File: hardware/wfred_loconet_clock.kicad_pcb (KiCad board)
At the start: 2 copper layers, 124 x 35 mm, 65 parts, among them IC201 ATMEGA328P-A, J301 Molex 95501-6669, K301 TERMINATION, K401 UART_ESP, K402 UART_AVR, P201 ISP, P401 ESP_BOOTLOAD, P501 CLOCK, Q301 BC817-40, Q302 BC817-40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

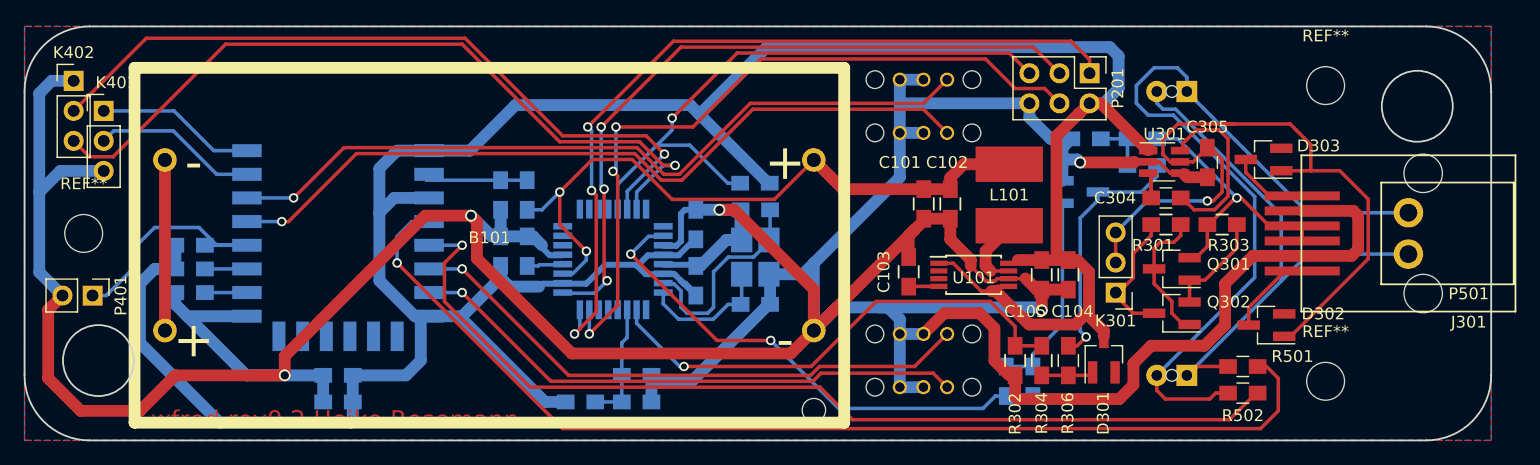
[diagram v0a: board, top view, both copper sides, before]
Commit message: Bugfix: Moved PCB mounting holes to correct corners
	(had been fitting for original FRED with UI on screw side,
	 which does not fit housing with battery cover)
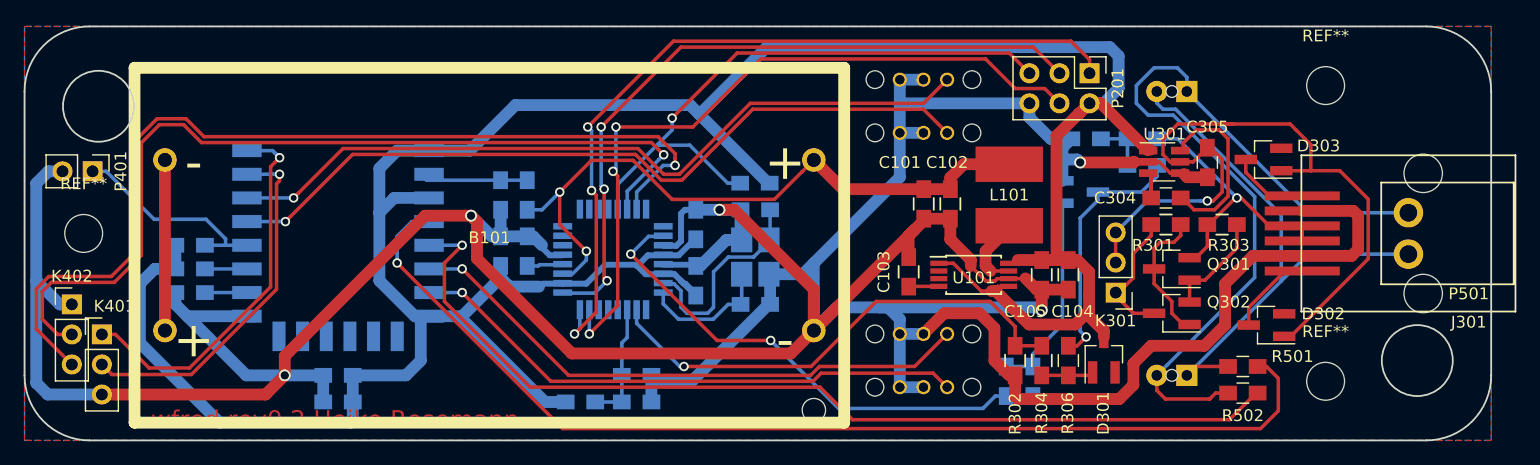
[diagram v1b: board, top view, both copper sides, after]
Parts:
- moved K401 18.9 mm to (76.5, 108.5)
- moved K402 18.9 mm to (74.0, 106.0)
- moved P401 10.5 mm to (75.8, 94.8)
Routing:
- net Net-(K401-Pad1): track 14.2 -> 32.5 mm, vias 0 -> 1
- net THIS_TXD: track 65.3 -> 81.0 mm
- net Net-(K401-Pad2): track 14.7 -> 30.0 mm, vias 0 -> 1
- net THIS_RXD: track 62.6 -> 76.3 mm
- net GND: track 393.8 -> 381.9 mm
- net Net-(P401-Pad1): track 22.0 -> 18.4 mm
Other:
- outline, holes or cut-outs redrawn

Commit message: Bugfix: Increased SW313 mounting hole clearance
	plus made GND fill distance to PCB edges larger for panelizing
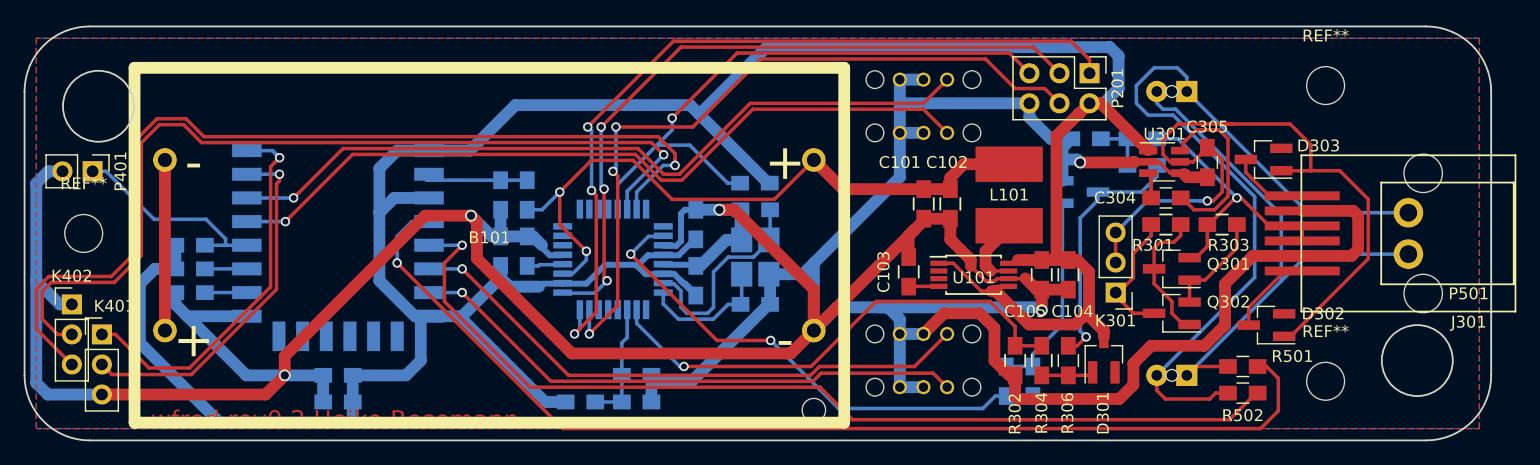
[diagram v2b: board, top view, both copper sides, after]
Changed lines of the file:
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@@
     (polygon
       (pts
-        (xy 70 82.5) (xy 70 117.5) (xy 194 117.5) (xy 194 82.5)
+        (xy 71 83.5) (xy 71 116.5) (xy 193 116.5) (xy 193 83.5)
       )
     )
@@
     (polygon
       (pts
-        (xy 194 82.5) (xy 194 117.5) (xy 70 117.5) (xy 70 82.5)
+        (xy 193 83.5) (xy 193 116.5) (xy 71 116.5) (xy 71 83.5)
       )
     )
